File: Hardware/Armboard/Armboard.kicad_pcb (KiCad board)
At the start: 2 copper layers, 124.8 x 100.4 mm, 111 parts, among them J1 Test_Point, SW1 SW_Push, SW2 SW_Push, SW3 SW_Push, SW4 SW_Push, SW5 SW_Push, SW6 SW_Push, U1 LM2576D2TR4, U2 TM4C129E_Launchpad

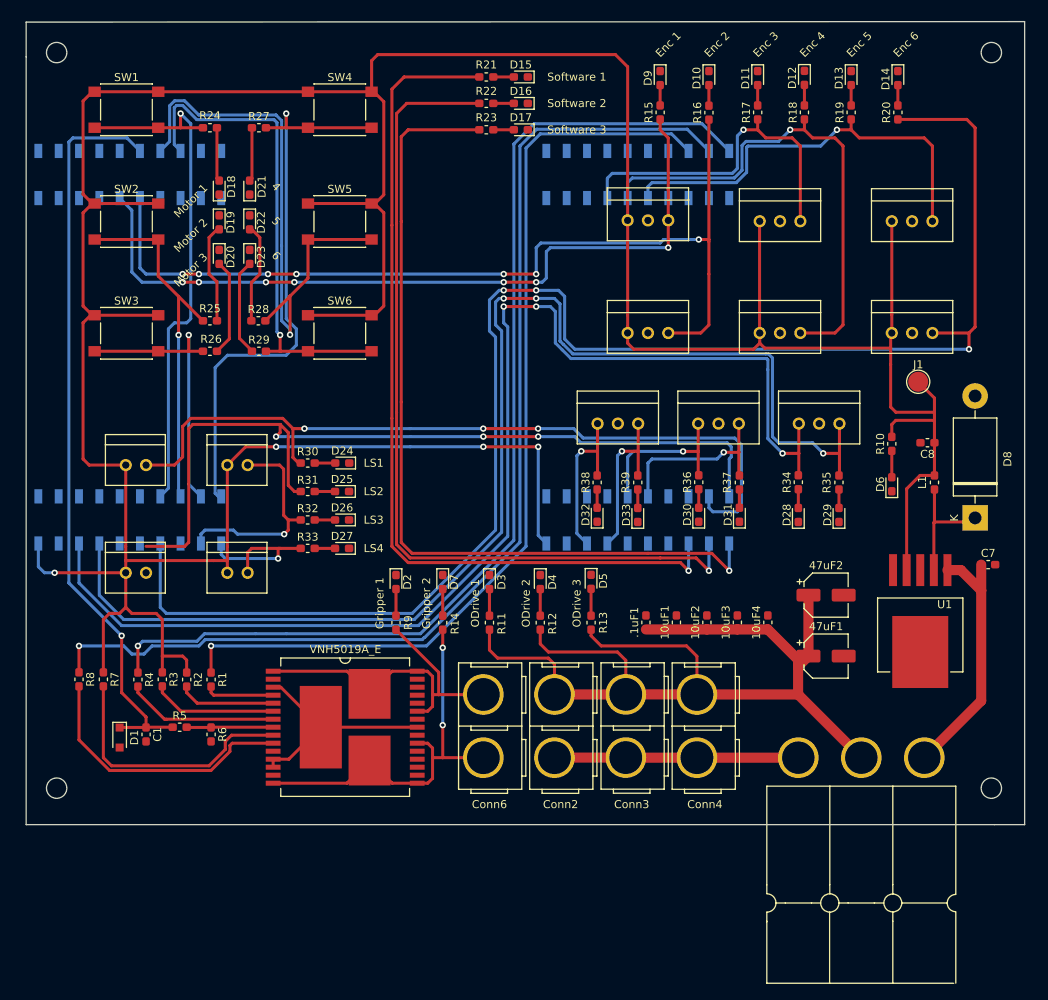
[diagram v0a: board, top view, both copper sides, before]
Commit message: Added ground planes
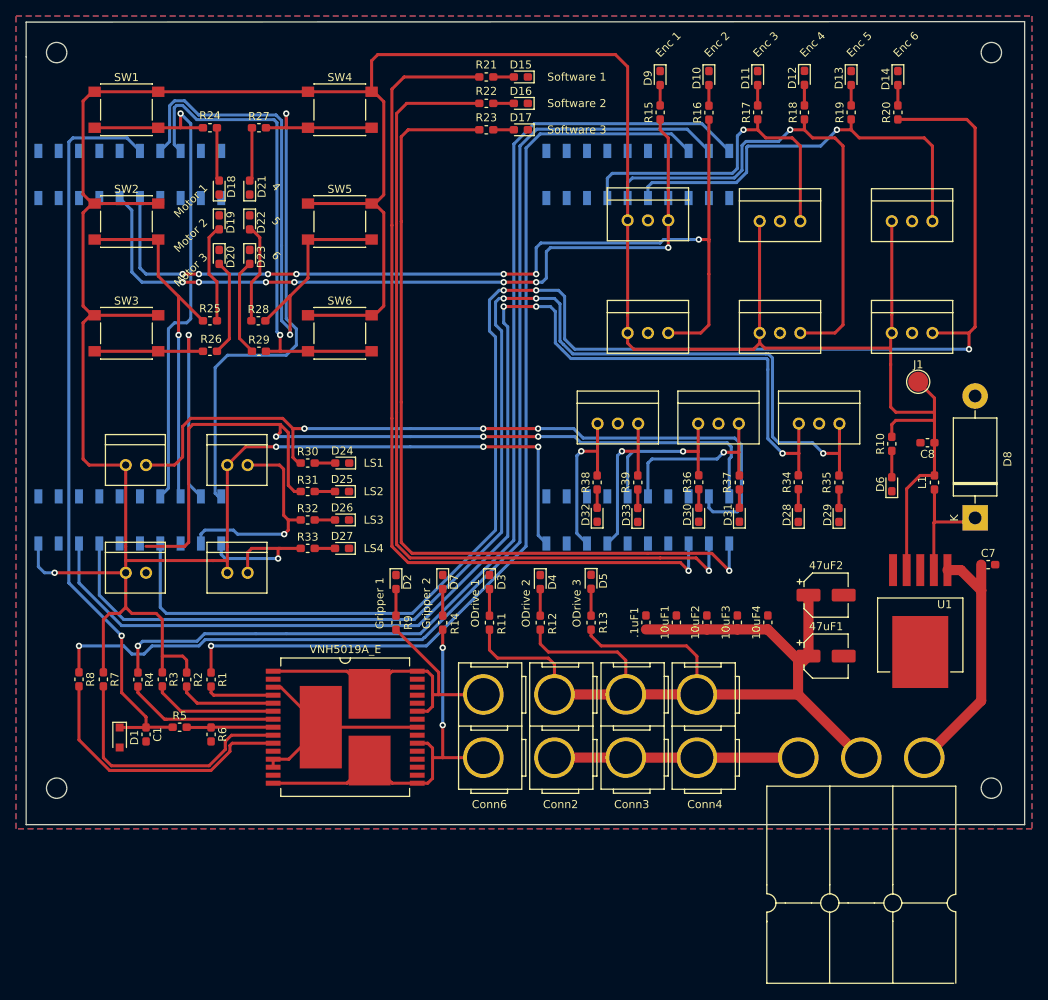
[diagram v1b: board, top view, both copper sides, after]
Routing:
- added copper zone on B.Cu, net GND
- added copper zone on F.Cu, net GND

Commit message: Started updating layout. Connected edge cuts
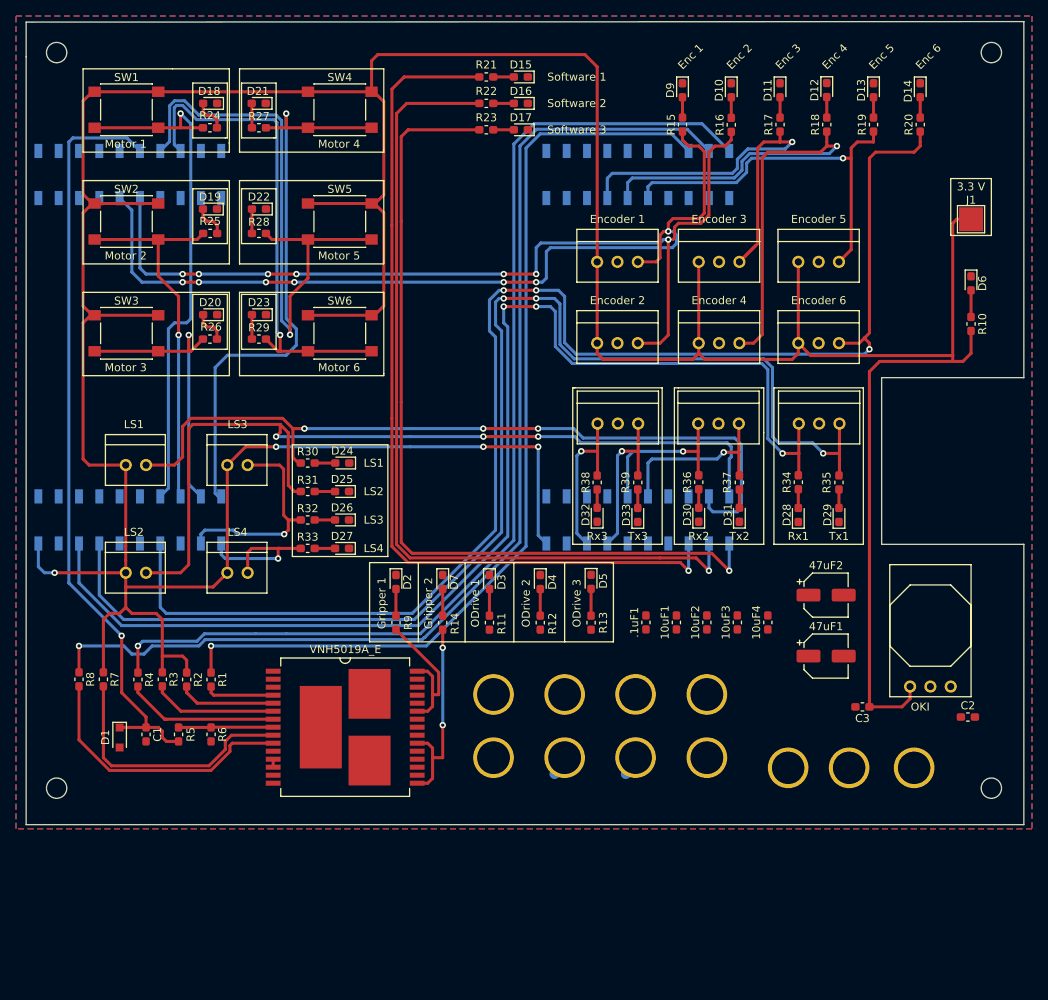
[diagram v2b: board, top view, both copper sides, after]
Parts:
- removed C7: 100uF, Capacitor_SMD:C_0603_1608Metric_Pad1.05x0.95mm_HandSolder
- removed C8: 1000uF, Capacitor_SMD:C_0603_1608Metric_Pad1.05x0.95mm_HandSolder
- removed D8: D_Schottky, Diode_THT:D_DO-201AD_P15.24mm_Horizontal
- removed L1: 100uH, Inductor_SMD:L_0603_1608Metric_Pad1.05x0.95mm_HandSolder
- added C2: 10uF, Capacitor_SMD:C_0603_1608Metric_Pad1.05x0.95mm_HandSolder, F.Cu at (192.6, 125.7)
- added C3: 10uF, Capacitor_SMD:C_0603_1608Metric_Pad1.05x0.95mm_HandSolder, F.Cu at (179.5, 124.5)
- Conn1, Conn2, Conn3, Conn4, Conn6: moved to B.Cu
- J1: footprint TestPoint:TestPoint_Pad_D2.5mm -> TestPoint:TestPoint_Pad_3.0x3.0mm
- U1: value LM2576D2TR4 -> OKI; footprint MRDT_Devices:LM2576 -> MRDT_Devices:OKI_Horizontal
- moved D6 27.0 mm to (193.0, 71.5), turned to 270 degrees
- moved J1 21.4 mm to (193.0, 63.5)
- moved R10 18.0 mm to (193.0, 76.6), turned to 270 degrees
- moved Conn1 14.5 mm to (185.9, 132.1)
- moved Conn12 12.7 mm to (171.4, 68.8)
- moved Conn13 11.8 mm to (171.4, 79.0)
- moved R28 10.9 mm to (104.0, 65.3)
- moved R25 10.9 mm to (97.9, 65.3)
- moved D18 10.6 mm to (97.9, 49.0), turned to 180 degrees
- moved D21 10.6 mm to (104.0, 49.0), turned to 180 degrees
- moved Conn10 9.16 mm to (159.0, 68.8)
- moved U1 9.07 mm to (190.5, 121.9)
- moved Conn11 7.73 mm to (159.0, 79.0)
- moved D23 7.32 mm to (104.0, 75.4), turned to 180 degrees
- moved D20 7.31 mm to (97.9, 75.4), turned to 180 degrees
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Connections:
- Conn1 pad 2: /Power/12V -> +12V
- Gripper_Motor1 pad 12: +12VA -> +12V
- Gripper_Motor1 pad 13: +12VA -> +12V
- Gripper_Motor1 pad 23: +12VA -> +12V
- Gripper_Motor1 pad 3: +12VA -> +12V
- Gripper_Motor1 pad 32: +12VA -> +12V
- U1 pad 1: /Power/12V -> +12V
- U1 pad 2: Net-(D8-Pad1) -> GND
- U1 pad 3: GND -> +3V3
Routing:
- net /Power/12VA: track 128.6 -> 0.00 mm
- net +3V3: track 473.9 -> 514.2 mm
- net /Power/12V: track 32.3 -> 0.00 mm
- net GND: track 30.5 -> 0.04 mm
- net +12VA: track 28.7 -> 0.00 mm
- net /H-Bridge/Gripper1: track 45.2 -> 19.2 mm
- net /H-Bridge/Gripper2: track 50.8 -> 25.4 mm
- net Enc_6_PWM: track 192.9 -> 175.2 mm
- net Net-(D8-Pad1): track 15.4 -> 0.00 mm
- net Enc_1_PWM: track 97.8 -> 109.9 mm
- net Net-(D22-Pad2): track 12.5 -> 3.05 mm
- net Enc_3_PWM: track 43.0 -> 52.1 mm
- net Net-(D23-Pad2): track 12.2 -> 3.20 mm
- net Net-(D19-Pad2): track 12.5 -> 4.23 mm
- net Net-(D20-Pad2): track 12.1 -> 4.21 mm
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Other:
- board size 124.8 x 100.4 mm -> 124.7 x 100.4 mm
- board text added: "3.3 V"
- board text added: "Encoder 1"
- board text added: "Encoder 2"
- board text added: "Encoder 3"
- board text added: "Encoder 4"
- board text added: "Encoder 5"
- board text added: "Encoder 6"
- board text added: "Motor 4"
- board text added: "Motor 5"
- board text added: "Motor 6"
- board text added: "Rx1"
- board text added: "Rx2"
- board text added: "Rx3"
- board text added: "Tx1"
- board text added: "Tx2"
- board text added: "Tx3"
- board text removed: "4"
- board text removed: "5"
- board text removed: "6"

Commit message: Routed 12VL and 12VA zones. Done?
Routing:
- net GND: track 0.04 -> 36.9 mm, vias 0 -> 38
- net +12V: track 1.00 -> 12.8 mm, vias 0 -> 41
- net /H-Bridge/Gripper2: track 25.4 -> 30.6 mm, vias 2 -> 16
- net /H-Bridge/Gripper1: track 19.2 -> 20.3 mm, vias 0 -> 20
- net Software_3: track 106.7 -> 105.6 mm
- net Software_2: track 108.5 -> 107.5 mm
- net Software_1: track 110.5 -> 109.4 mm
- net Enc_6_PWM: track 175.2 -> 175.9 mm
- net Tx_1_Tiva: track 157.3 -> 158.0 mm
- net /Power/12VA: vias 0 -> 37
- added copper zone on B.Cu, net +12V
- added copper zone on F.Cu, net +12V
- added copper zone on B.Cu, net /H-Bridge/Gripper1
- added copper zone on F.Cu, net /H-Bridge/Gripper1
- added copper zone on B.Cu, net /H-Bridge/Gripper2
- added copper zone on F.Cu, net /H-Bridge/Gripper2
- added copper zone on B.Cu, net /Power/12VA
- added copper zone on F.Cu, net /Power/12VA

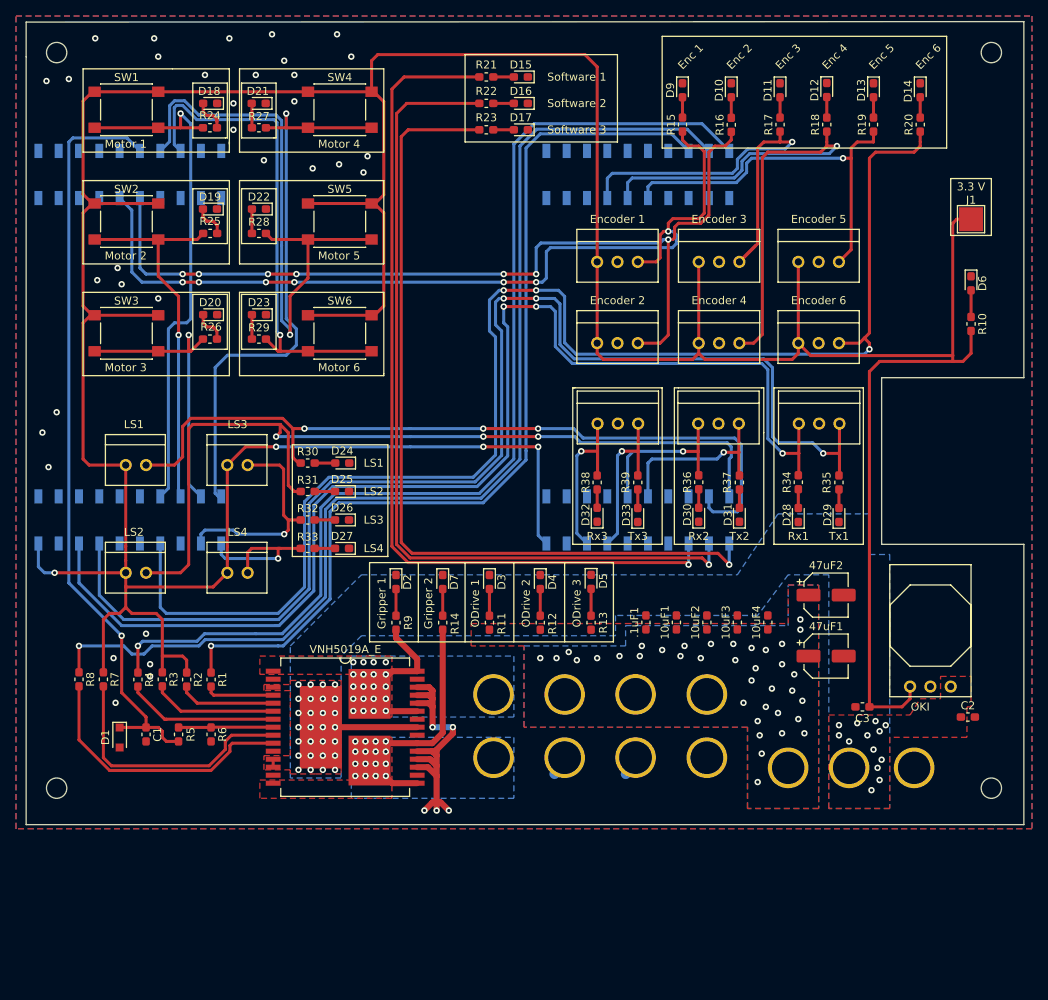
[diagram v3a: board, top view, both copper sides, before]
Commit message: Rounded edge cuts, added silkscreen header
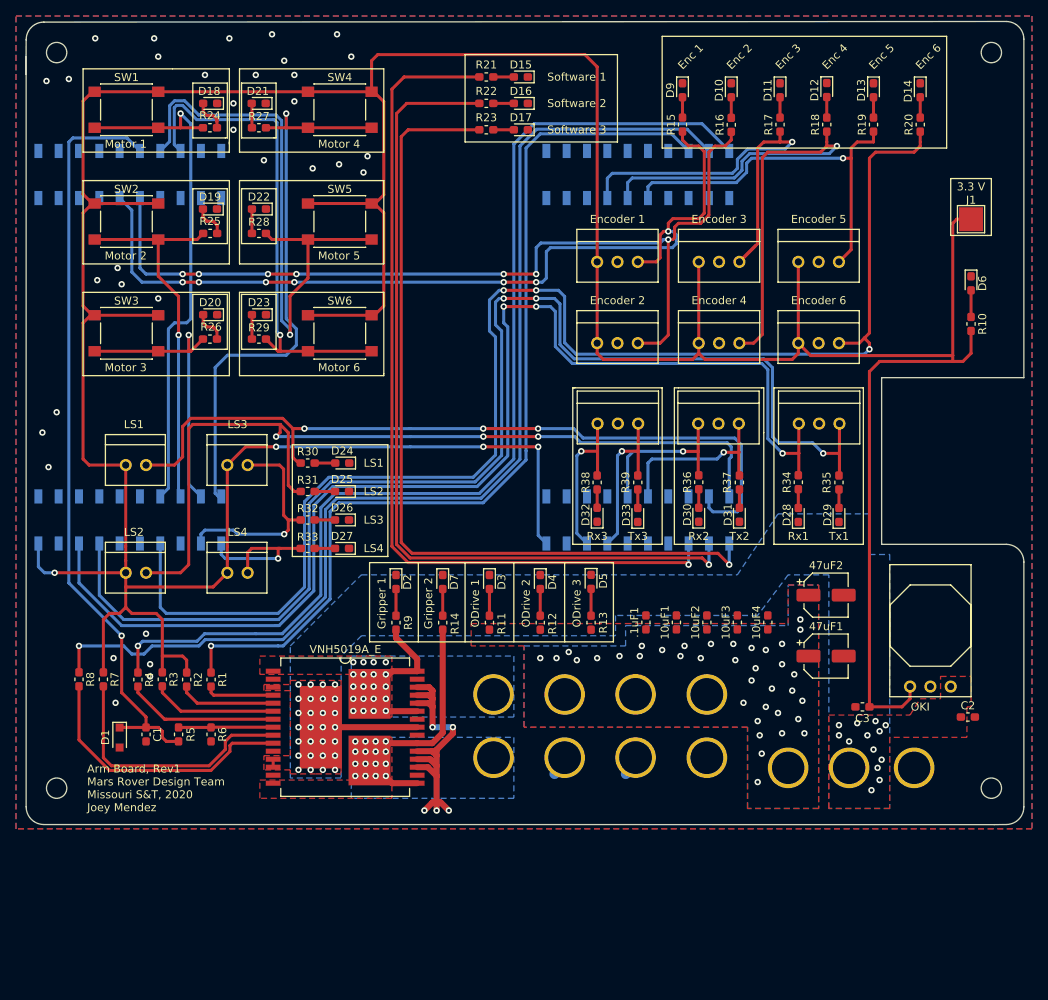
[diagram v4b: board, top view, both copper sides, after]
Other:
- outline, holes or cut-outs redrawn
- board text added: "Arm Board, Rev1 Mars Rover Design Team Missouri S&T, 2020 Joey Mendez"

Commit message: Added silkscreen designs
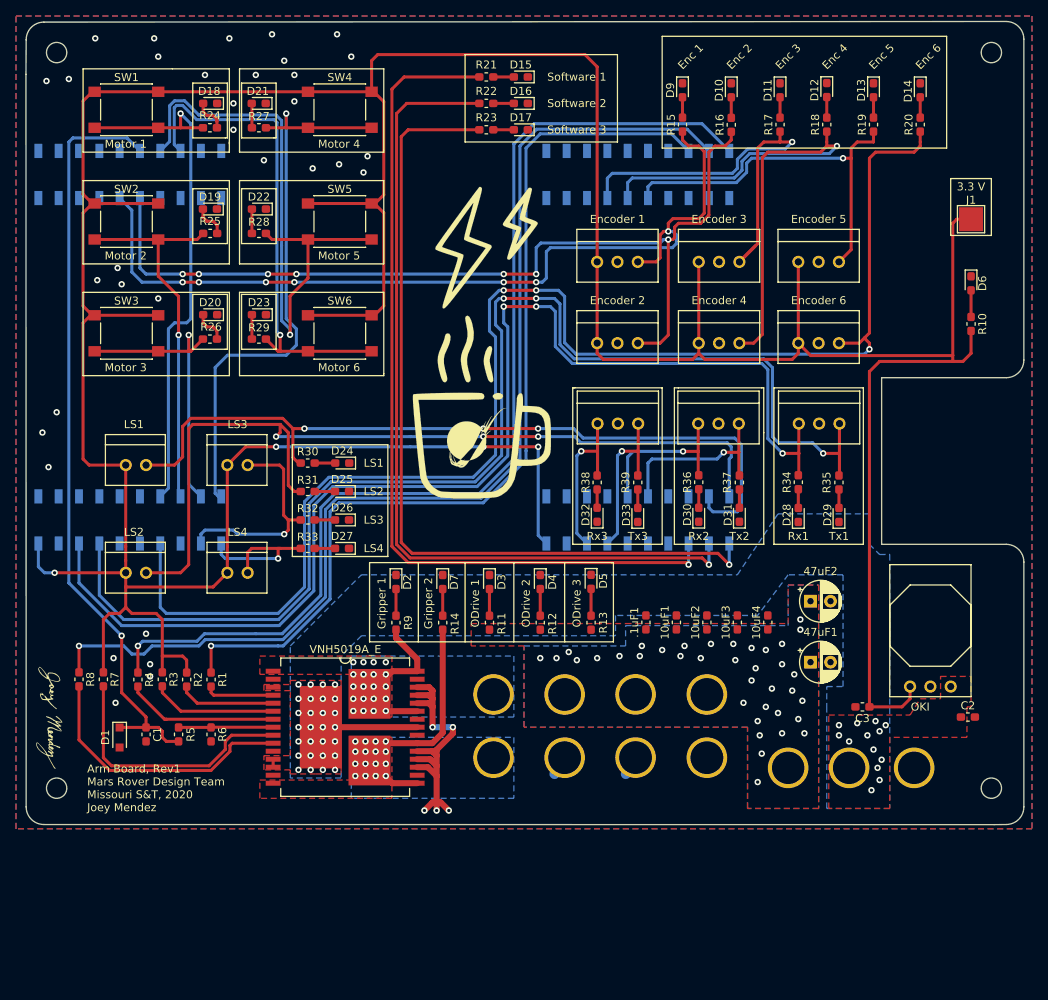
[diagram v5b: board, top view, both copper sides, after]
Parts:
- added G***: LOGO, Project Library:lightning_bolt_15mm, F.Cu at (132.5, 67.1)
- added G***: LOGO, MRDT_Silkscreens:0_MRDT_Logo_7.5mm, F.Cu at (131.3, 90.8)
- added G***: LOGO, Project Library:coffee_time_20mm, F.Cu at (131.8, 87.0)
- added G***: LOGO, Project Library:signature_14.6mmx6.5mm, F.Cu at (78.0, 125.7)
- 47uF1, 47uF2: footprint Capacitor_SMD:CP_Elec_5x5.4 -> Capacitor_THT:CP_Radial_D5.0mm_P2.50mm
- moved 47uF1 2.09 mm to (173.0, 118.9)
- moved 47uF2 2.09 mm to (173.0, 111.3)
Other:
- outline, holes or cut-outs redrawn

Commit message: Added more labels, fixed 12VA/12L connections, filled gnd islands, +/-/S labels, added drillhole footprints
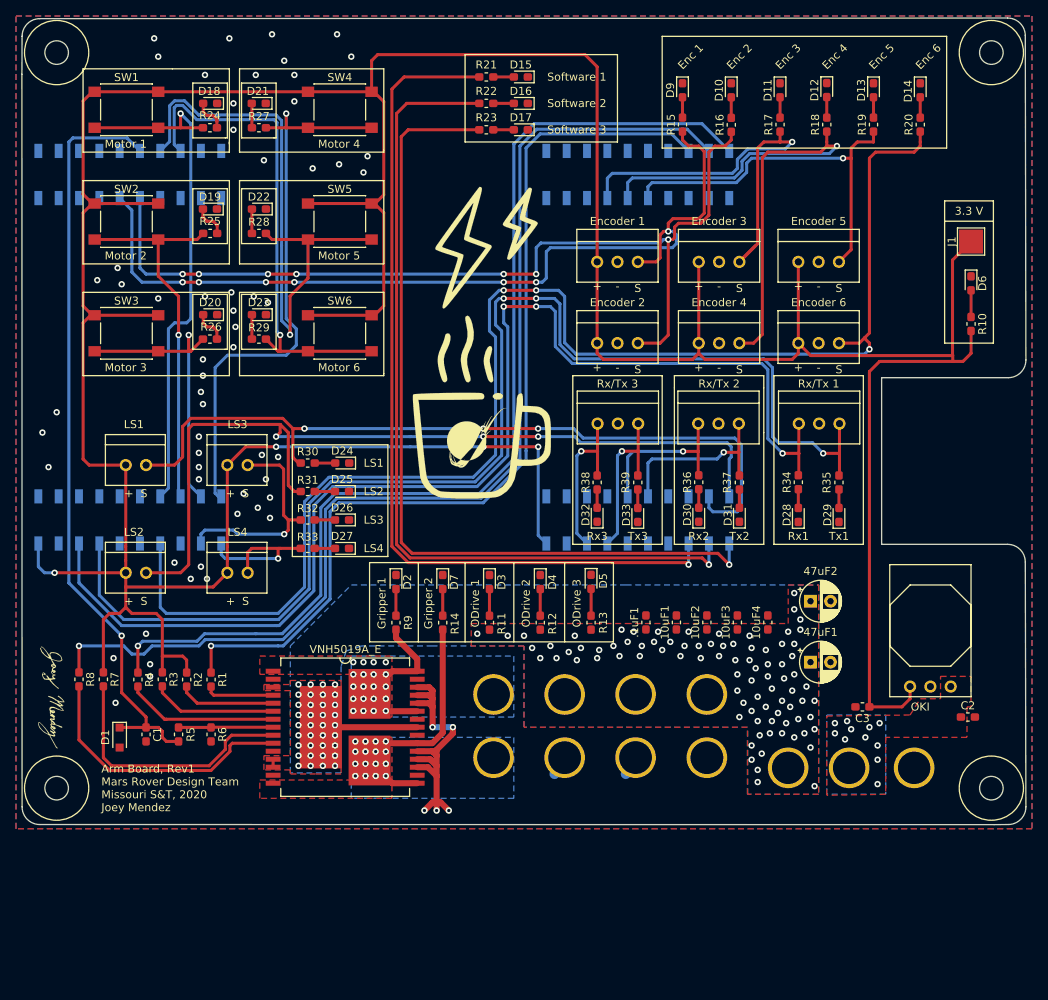
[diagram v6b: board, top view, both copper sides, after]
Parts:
- added REF**: 4_40_Hole, MRDT_Drill_Holes:4_40_Hole_Corner, F.Cu at (191.6, 46.7)
- added REF**: 4_40_Hole, MRDT_Drill_Holes:4_40_Hole_Corner, F.Cu at (82.7, 46.7)
- added REF**: 4_40_Hole, MRDT_Drill_Holes:4_40_Hole_Corner, F.Cu at (82.7, 130.6)
- added REF**: 4_40_Hole, MRDT_Drill_Holes:4_40_Hole_Corner, F.Cu at (191.6, 130.6)
- moved J1 2.79 mm to (193.0, 66.3), turned to 90 degrees
- moved G*** 2.55 mm to (78.2, 123.2)
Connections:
- .1uF1 pad 1: /Power/12VA -> +12V
- 10uF1 pad 1: /Power/12VA -> +12V
- 10uF2 pad 1: /Power/12VA -> +12V
- 10uF3 pad 1: /Power/12VA -> +12V
- 10uF4 pad 1: /Power/12VA -> +12V
- 47uF1 pad 1: /Power/12VA -> +12V
- 47uF2 pad 1: /Power/12VA -> +12V
- C2 pad 1: +12V -> +12L
- Conn1 pad 2: +12V -> +12L
- Conn1 pad 3: /Power/12VA -> +12V
- Conn2 pad 2: /Power/12VA -> +12V
- Conn3 pad 2: /Power/12VA -> +12V
- Conn4 pad 2: /Power/12VA -> +12V
- R11 pad 1: /Power/12VA -> +12V
- R12 pad 1: /Power/12VA -> +12V
- R13 pad 1: /Power/12VA -> +12V
- U1 pad 1: +12V -> +12L
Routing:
- net +3V3: track 514.2 -> 510.4 mm
- net GND: vias 38 -> 58
- net /Power/12VA: vias 37 -> 0
- net +12V: vias 41 -> 123
- net +12L: vias 0 -> 11
- net (no net): vias 0 -> 4
- added copper zone on B.Cu, net +12L
- added copper zone on F.Cu, net +12L
- removed copper zone on B.Cu, net /Power/12VA
- removed copper zone on F.Cu, net /Power/12VA
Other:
- board size 124.7 x 100.4 mm -> 125.5 x 100.8 mm
- board text added: "+"
- board text added: "+ S"
- board text added: "-"
- board text added: "Rx/Tx 1"
- board text added: "Rx/Tx 2"
- board text added: "Rx/Tx 3"
- board text added: "S"

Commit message: vias
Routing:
- net GND: vias 58 -> 467
- net +12V: vias 123 -> 134
- net +12L: vias 11 -> 13
